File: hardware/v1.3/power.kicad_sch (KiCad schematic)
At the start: 48 parts, among them U1 ECP5-CABGA256, U2 TLV62569DBV, U3 TLV62569DBV, U4 TLV62569DBV

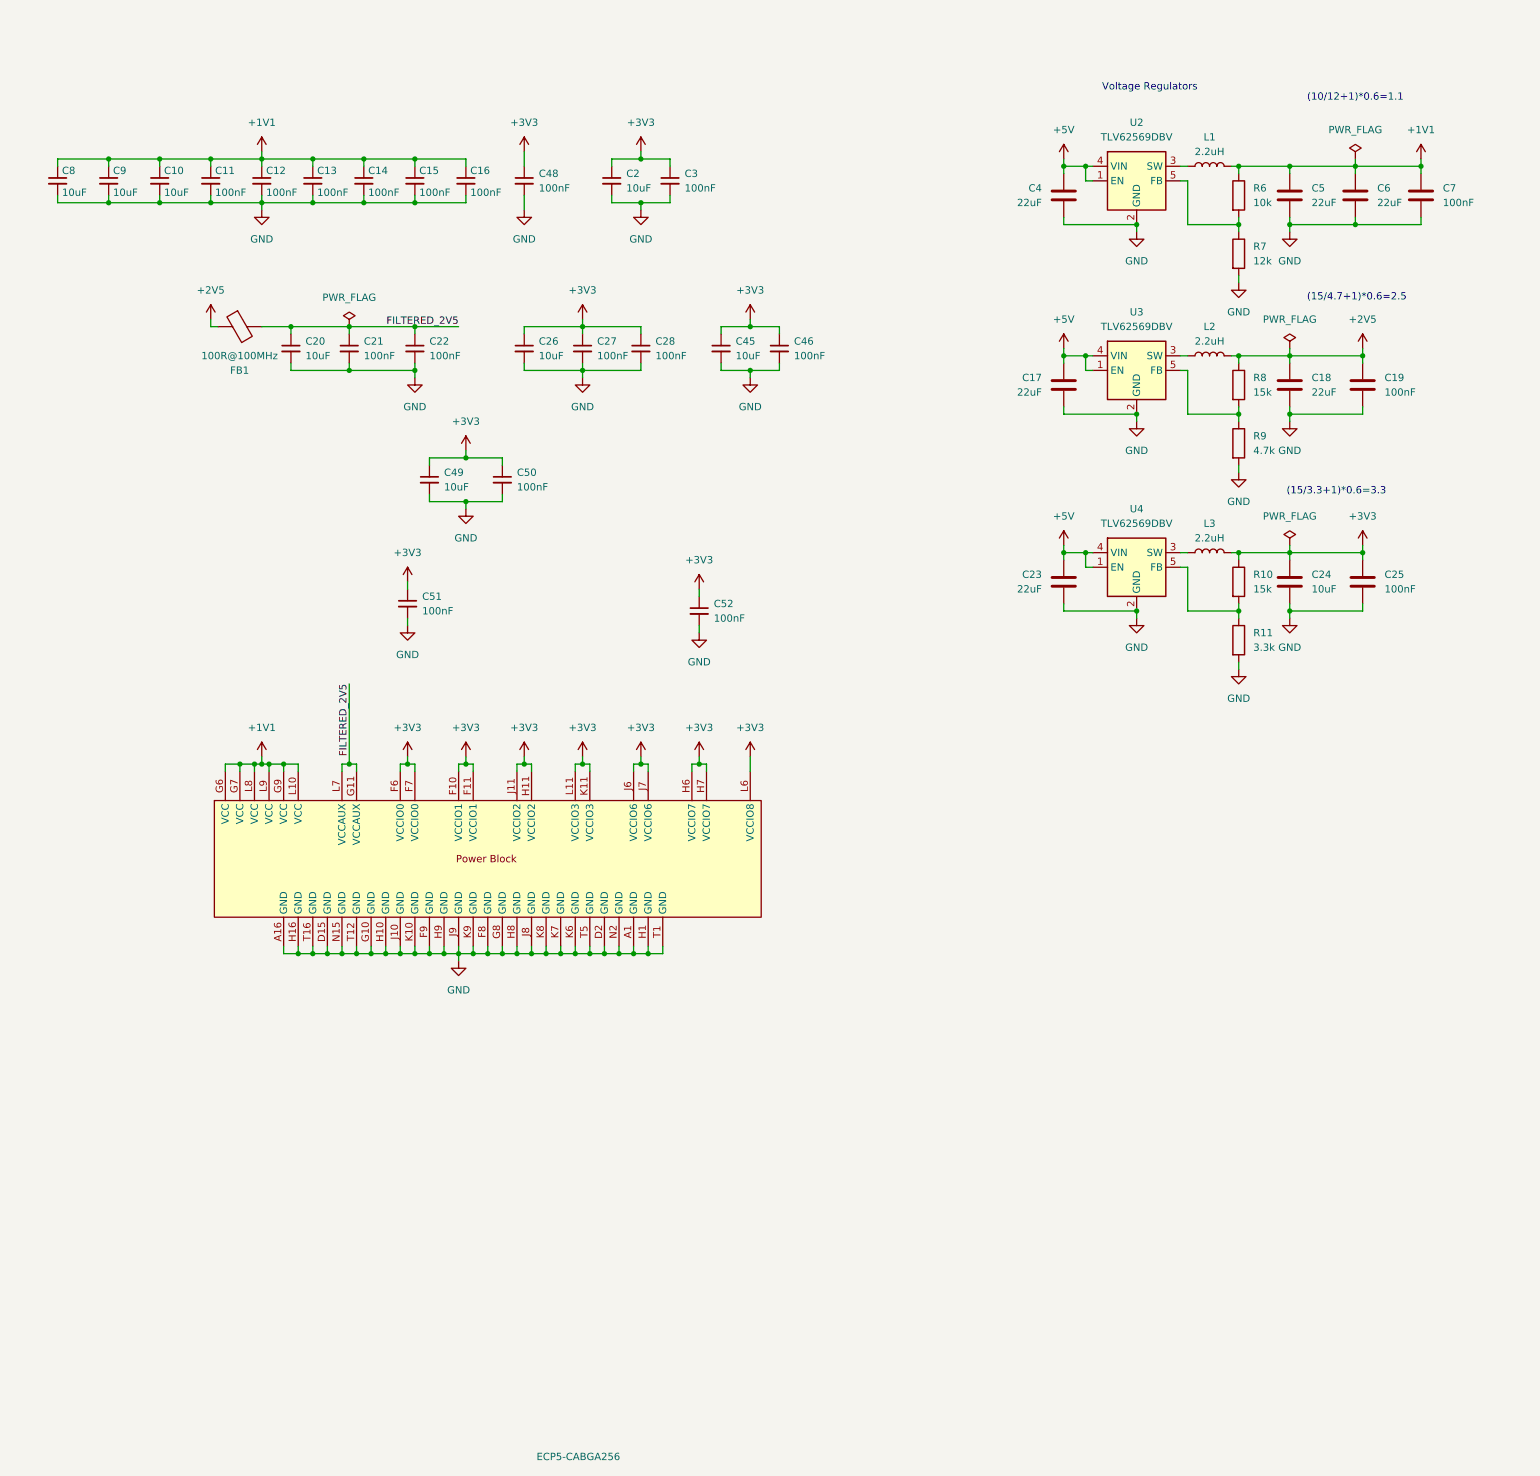
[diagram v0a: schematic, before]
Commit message: Refine README
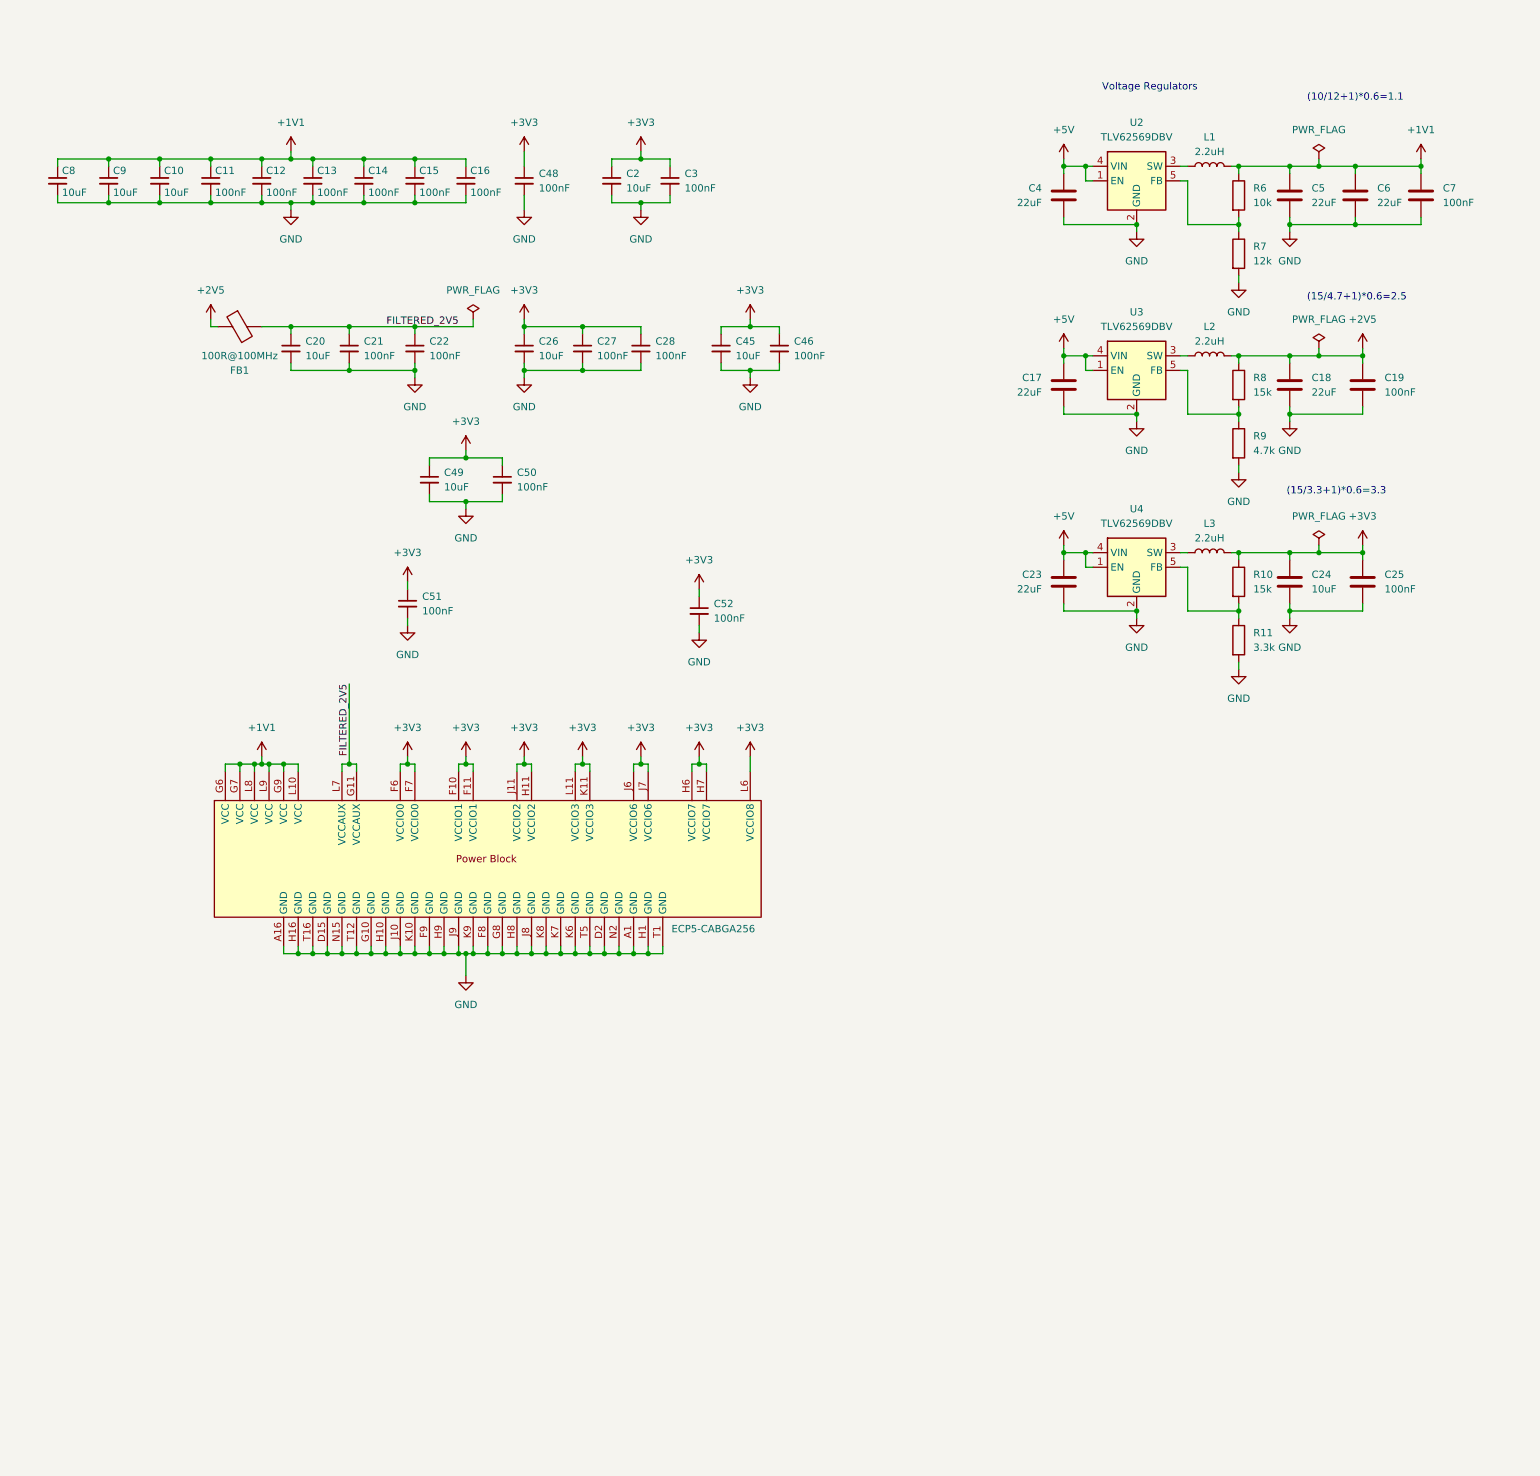
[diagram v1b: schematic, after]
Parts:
- C10, C2, C20, C24, C26, C45, C49, C8, C9: LCSC Link (none) -> https://lcsc.com/product-detail/Multilayer-Ceramic-Capacito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; Manufactuer Part Number (none) -> CL10A106KP8NNNC
- C11, C12, C13, C14, C15, C16, C19, C21, C22, C25, C27, C28, C3, C46, C48, C50, C51, C52, C7: LCSC Link (none) -> https://lcsc.com/product-detail/Multilayer-Ceramic-Capacito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; LCSC Part # C307331 -> C307331; Manufactuer Part Number (none) -> CL05B104KB54PNC
- C17, C18, C23, C4, C5, C6: LCSC Link (none) -> https://lcsc.com/product-detail/Multilayer-Ceramic-Capacito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; LCSC Part # C59461 -> C59461; Manufactuer Part Number (none) -> CL10A226MQ8NRNC
- FB1: LCSC Link (none) -> https://lcsc.com/product-detail/Ferrite-Beads_FH-CBG201209U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; LCSC Part # C1015 -> C74480; Manufactuer Part Number (none) -> CBG201209U101T
- L1, L2, L3: LCSC Link (none) -> https://lcsc.com/product-detail/Inductors-SMD_FH-CMI201209U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; Manufactuer Part Number (none) -> CMI201209U2R2KT
- R10, R8: LCSC Link (none) -> https://lcsc.com/product-detail/Chip-Resistor-Surface-Mount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; Manufactuer Part Number (none) -> 0402WGF1502TCE
- R11: LCSC Link (none) -> https://lcsc.com/product-detail/Chip-Resistor-Surface-Mount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; LCSC Part # C25890 -> C25890; Manufactuer Part Number (none) -> 0402WGF3301TCE
- R6: LCSC Link (none) -> https://lcsc.com/product-detail/Chip-Resistor-Surface-Mount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; Manufactuer Part Number (none) -> 0402WGF1002TCE
- R7: LCSC Link (none) -> https://lcsc.com/product-detail/Chip-Resistor-Surface-Mount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; Manufactuer Part Number (none) -> 0402WGF1202TCE
- R9: LCSC Link (none) -> https://lcsc.com/product-detail/Chip-Resistor-Surface-Mount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; LCSC Part # C25900 -> C25900; Manufactuer Part Number (none) -> 0402WGF4701TCE
- U1: LCSC Link (none) -> https://lcsc.com/product-detail/Programmable-Logic-Device-C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; LCSC Part # (none) -> C1521614; Manufactuer Part Number (none) -> LFE5U-25F-6BG256C
- U2, U3, U4: LCSC Link (none) -> https://lcsc.com/product-detail/DC-DC-Converters_TI-TLV6256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; Manufactuer Part Number (none) -> TLV62569DBVR

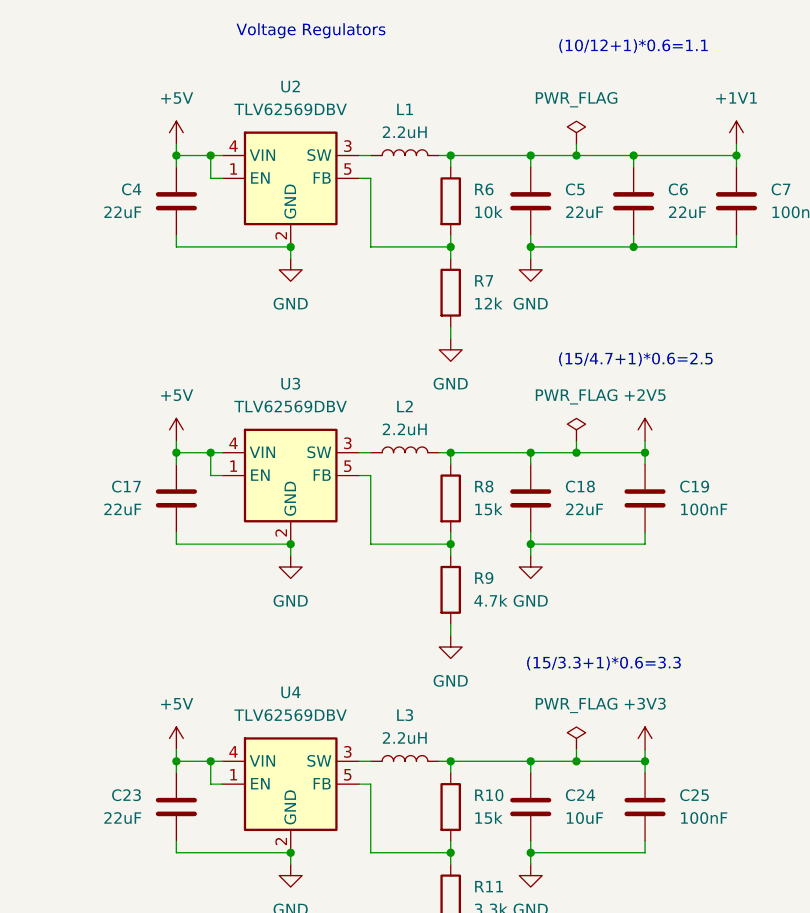
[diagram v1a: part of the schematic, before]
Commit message: Change to more optimal inductor
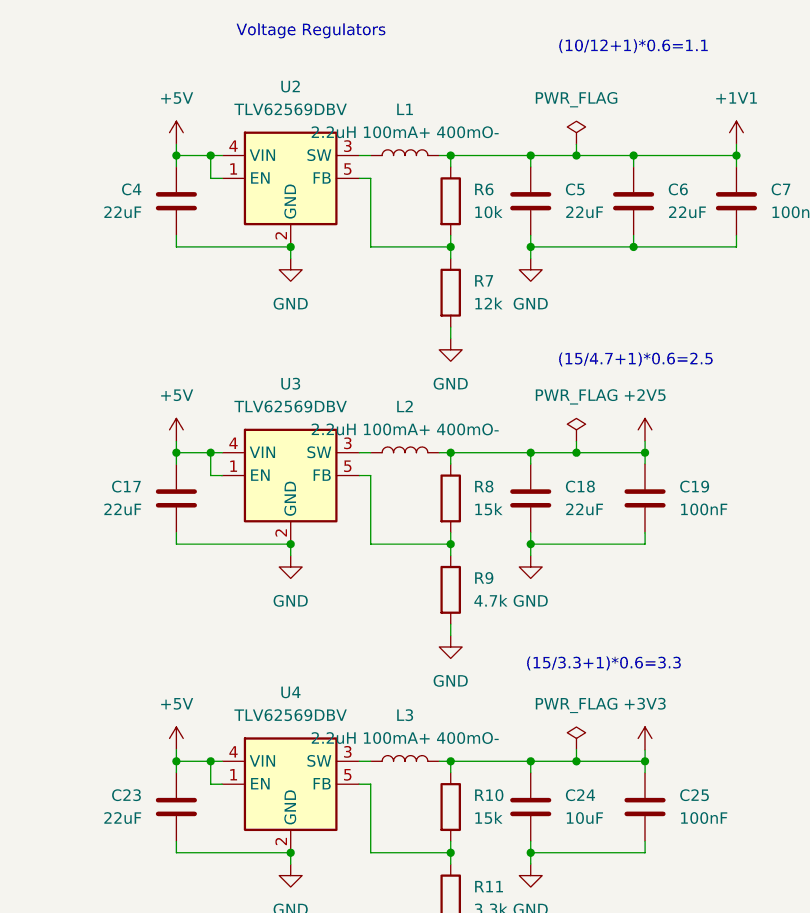
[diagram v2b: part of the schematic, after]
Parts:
- L1, L2, L3: value 2.2uH -> 2.2uH 100mA+ 400mO-; LCSC Link https://lcsc.com/product-detail/Inductors-SMD_FH-CMI201209U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 -> https://lcsc.com/product-detail/C107322.html; LCSC Part # C1043 -> C107322; Manufactuer Part Number CMI201209U2R2KT -> TDK MLP2012S2R2MT0S1
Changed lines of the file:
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@@
 			)
 		)
-		(property "Value" "2.2uH"
+		(property "Value" "2.2uH 100mA+ 400mO-"
 			(at 229.87 104.14 90)
 			(effects
@@
 			)
 		)
-		(property "LCSC Part #" "C1043"
+		(property "LCSC Part #" "C107322"
 			(at 229.87 106.68 0)
 			(effects
@@
 			)
 		)
-		(property "LCSC Link" "https://lcsc.com/product-detail/Inductors-SMD_FH-CMI201209U2R2KT_C1043.html"
+		(property "LCSC Link" "https://lcsc.com/product-detail/C107322.html"
 			(at 229.87 106.68 90)
 			(effects
@@
 			)
 		)
-		(property "Manufactuer Part Number" "CMI201209U2R2KT"
+		(property "Manufactuer Part Number" "TDK MLP2012S2R2MT0S1"
 			(at 229.87 106.68 90)
 			(effects
@@
 			)
 		)
-		(property "Value" "2.2uH"
+		(property "Value" "2.2uH 100mA+ 400mO-"
 			(at 229.87 36.83 90)
 			(effects
@@
 			)
 		)
-		(property "LCSC Part #" "C1043"
+		(property "LCSC Part #" "C107322"
 			(at 229.87 39.37 0)
 			(effects
@@
 			)
 		)
-		(property "LCSC Link" "https://lcsc.com/product-detail/Inductors-SMD_FH-CMI201209U2R2KT_C1043.html"
+		(property "LCSC Link" "https://lcsc.com/product-detail/C107322.html"
 			(at 229.87 39.37 90)
 			(effects
@@
 			)
 		)
-		(property "Manufactuer Part Number" "CMI201209U2R2KT"
+		(property "Manufactuer Part Number" "TDK MLP2012S2R2MT0S1"
 			(at 229.87 39.37 90)
 			(effects
@@
 			)
 		)
-		(property "Value" "2.2uH"
+		(property "Value" "2.2uH 100mA+ 400mO-"
 			(at 229.87 69.85 90)
 			(effects
@@
 			)
 		)
-		(property "LCSC Part #" "C1043"
+		(property "LCSC Part #" "C107322"
 			(at 229.87 72.39 0)
 			(effects
@@
 			)
 		)
-		(property "LCSC Link" "https://lcsc.com/product-detail/Inductors-SMD_FH-CMI201209U2R2KT_C1043.html"
+		(property "LCSC Link" "https://lcsc.com/product-detail/C107322.html"
 			(at 229.87 72.39 90)
 			(effects
@@
 			)
 		)
-		(property "Manufactuer Part Number" "CMI201209U2R2KT"
+		(property "Manufactuer Part Number" "TDK MLP2012S2R2MT0S1"
 			(at 229.87 72.39 90)
 			(effects

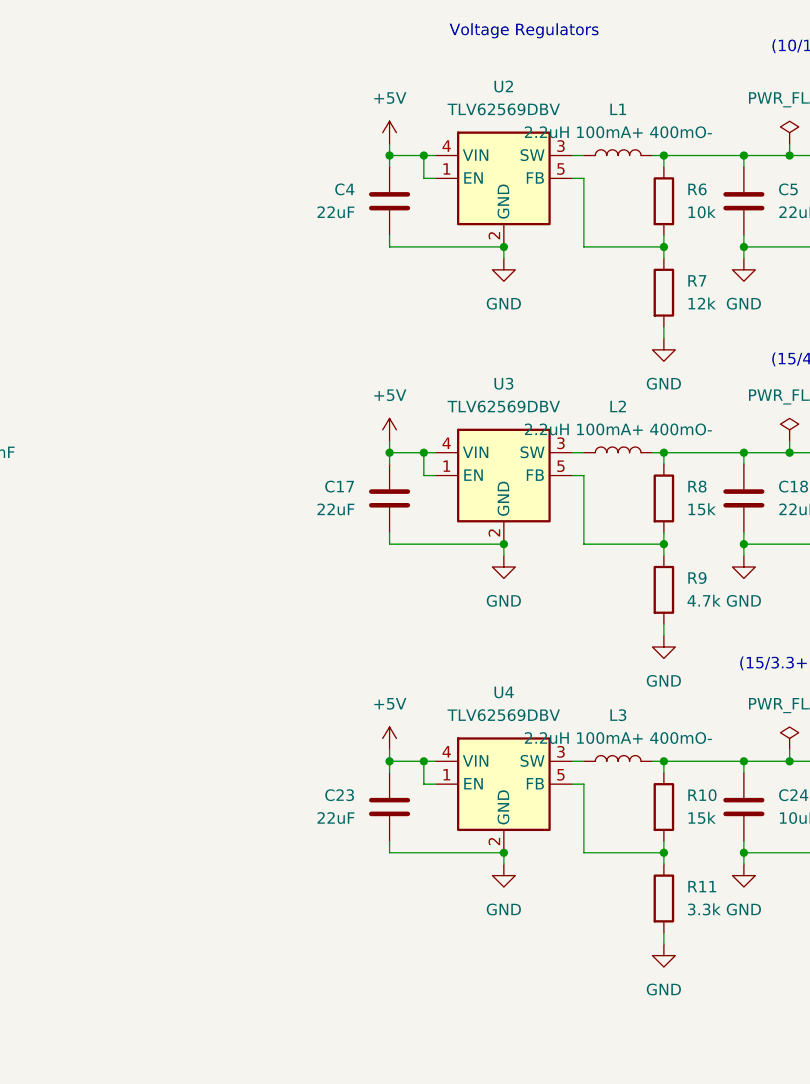
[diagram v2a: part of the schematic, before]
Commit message: Added start of documentation and changed GPDI
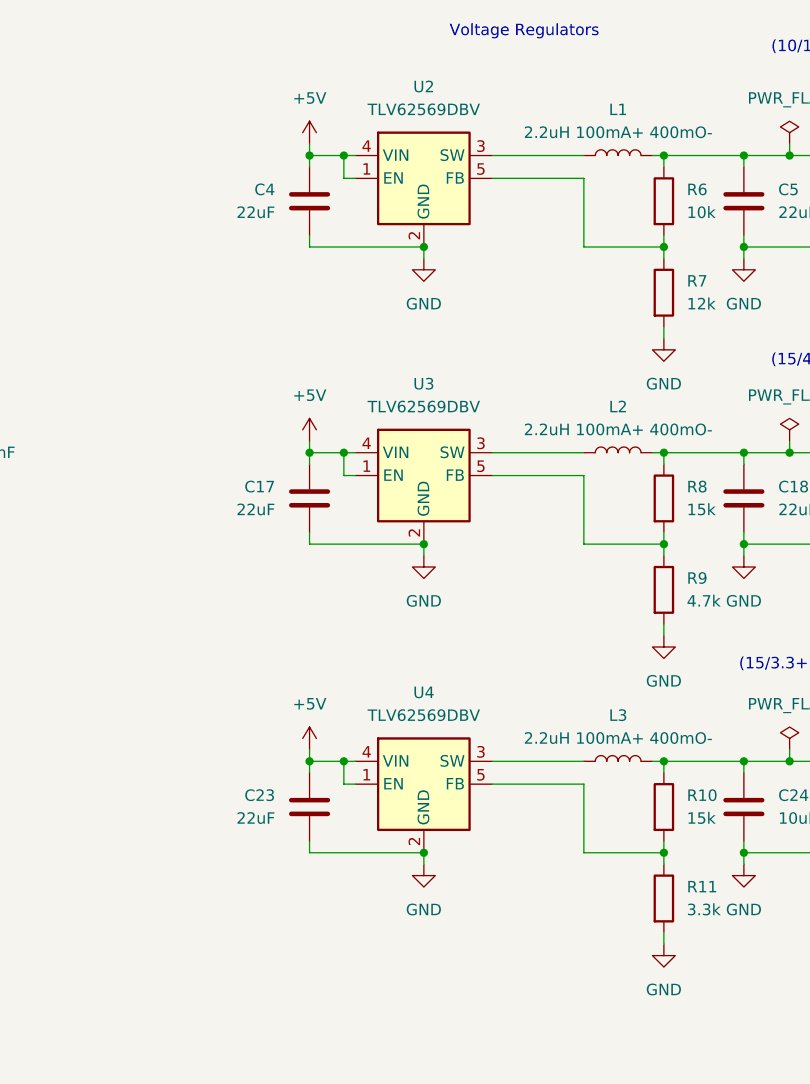
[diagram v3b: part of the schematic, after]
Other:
- moved on the sheet: C17, C23, C4, U2, U3, U4

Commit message: Update files
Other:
- note added: "(10/12+1)*0.6=1.1V"
- note added: "(15/3.3+1)*0.6=3.3V"
- note added: "(15/4.7+1)*0.6=2.5V"
- note added: "1x 10u and 1x 100n per I/O bank pin"
- note added: "Decoupling capacitors based on FPGA-TN-02038"
- note removed: "(10/12+1)*0.6=1.1"
- note removed: "(15/3.3+1)*0.6=3.3"
- note removed: "(15/4.7+1)*0.6=2.5"
- moved on the sheet: C10, C11, C12, C13, C14, C15, C16, C2, C20, C21, C22, C26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

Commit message: Update to v1.3 board
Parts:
- L1, L2, L3: Note (none) -> 2.2uH 100mA+ 400mO-; Notes (none) -> 2.2uH 100mA+ 400mO-
